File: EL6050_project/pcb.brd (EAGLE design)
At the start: 160 x 100 mm, 6 parts

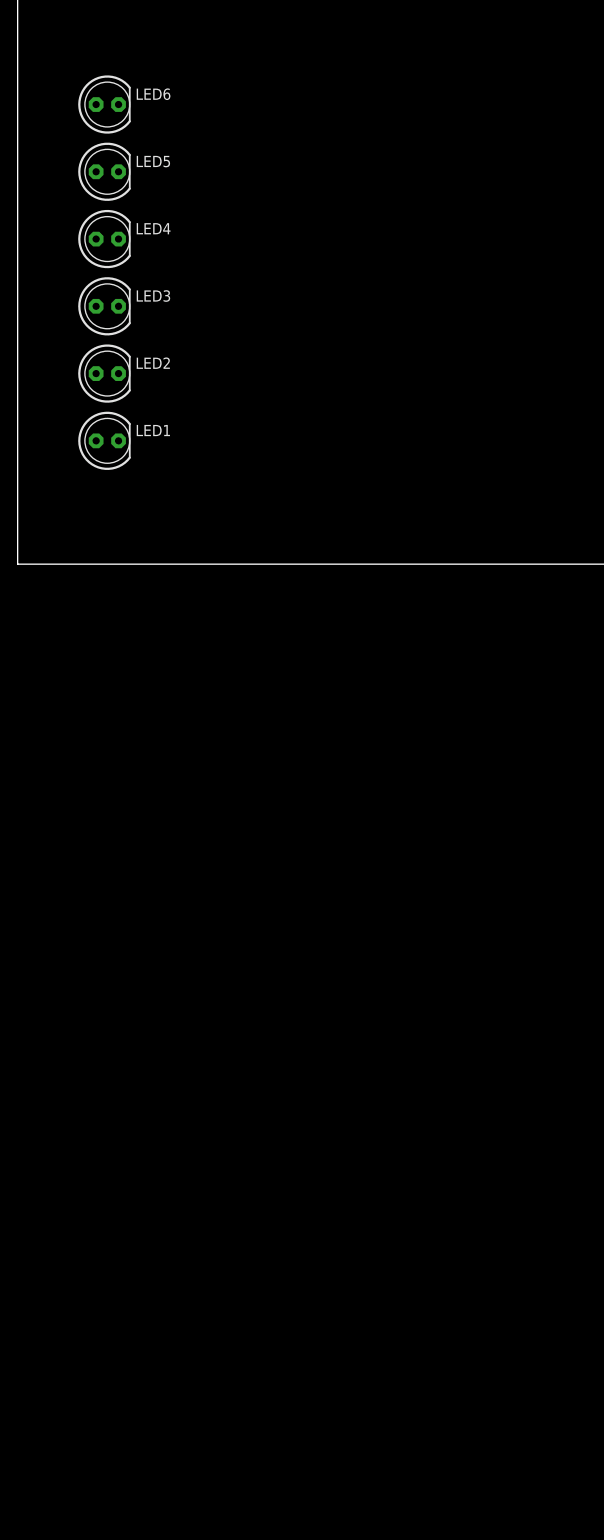
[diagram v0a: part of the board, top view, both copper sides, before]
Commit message: add lorawan module and arduino to schematic
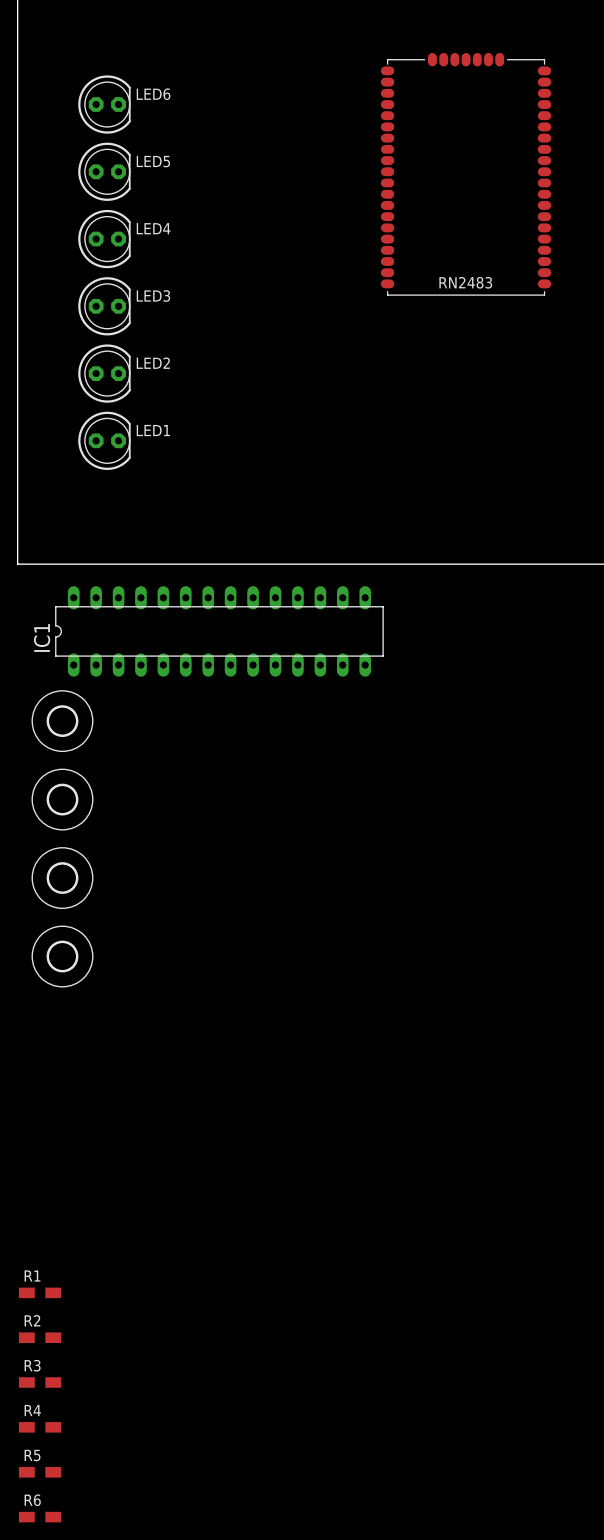
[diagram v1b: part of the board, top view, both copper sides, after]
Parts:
- added H1, H2, H3, H4: MOUNT-HOLE3.2, holes:3,2
- added IC1: MEGA8-P, atmel:DIL28-3
- added R1, R2, R3, R4, R5, R6: (no value), rcl:R1206W
- added U$1: MICROCHIP_RN2483, lora-lorawan-modules:MICROCHIP_RN2483
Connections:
- new net AVCC: IC1.20
- new net GND: IC1.22, IC1.8
- new net N$1: U$1.35
- new net N$10: U$1.39
- new net N$11: U$1.43
- new net N$12: U$1.45
- new net N$13: U$1.46
- new net N$14: U$1.10
- new net N$15: U$1.12, U$1.34
- new net N$16: U$1.32
- new net N$17: U$1.25
- new net N$18: U$1.3
- new net N$19: U$1.7
- new net N$2: U$1.36
- new net N$20: U$1.31
- new net N$21: U$1.1, U$1.11, U$1.20, U$1.21, U$1.22, U$1.24, U$1.26, U$1.27, U$1.28, U$1.33, U$1.41, U$1.47, U$1.8
- new net N$22: U$1.23
- new net N$23: U$1.2
- new net N$24: U$1.6
- new net N$25: U$1.30
- new net N$26: LED1.K
- new net N$27: LED2.K
- new net N$28: LED3.K
- new net N$29: LED4.K
- new net N$3: U$1.37
- new net N$30: LED5.K
- new net N$31: LED6.K
- new net N$32: LED1.A, R1.1
- new net N$33: LED2.A, R2.1
- new net N$34: LED3.A, R3.1
- new net N$35: LED4.A, R4.1
- new net N$36: LED5.A, R5.1
- new net N$37: LED6.A, R6.1
- new net N$38: IC1.23
- new net N$39: IC1.25
- new net N$4: U$1.38
- new net N$40: IC1.2
- new net N$41: IC1.4
- new net N$42: IC1.6
- new net N$43: IC1.12
- new net N$44: IC1.14
- new net N$45: IC1.17
- new net N$46: IC1.18
- new net N$47: IC1.27
- new net N$48: IC1.24
- new net N$49: IC1.26
- new net N$5: U$1.40
- new net N$50: IC1.28
- new net N$51: IC1.3
- new net N$52: IC1.5
- new net N$53: IC1.11
- new net N$54: IC1.13
- new net N$55: IC1.15
- new net N$56: IC1.16
- new net N$57: IC1.19
- new net N$6: U$1.44
- new net N$7: U$1.14
- new net N$8: U$1.13
- new net N$9: U$1.9
- new net VCC: IC1.7

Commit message: add and connect components
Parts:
- added C1, C2, C3, C4, C5, C6: (no value), rcl:C050-025X075
- added IC2: MEGA8-P, atmel:DIL28-3
- added Q1, Q2: (no value), crystal:HC18U-V
- added R10, R11, R7, R8: (no value), rcl:R1206W
- added R9: 10k, rcl:R1206W
- added SV1, SV2: (no value), con-lstb:MA03-1
- added X1: BU-SMA-V, con-coax:BU-SMA-V
- added X2: GMSTBA2, con-phoenix-762:GMSTBA2
- moved H1 150.3 mm to (146.1, 34.3)
- moved H2 150.3 mm to (146.1, 25.4)
- moved H3 150.3 mm to (146.1, 16.5)
- moved H4 150.3 mm to (146.1, 7.62)
- moved R4 131.8 mm to (26.7, 31.8)
- moved R5 131.8 mm to (26.7, 26.7)
- moved R1 131.8 mm to (26.7, 47.0)
- moved R2 131.8 mm to (26.7, 41.9)
- moved R3 131.8 mm to (26.7, 36.8)
- moved R6 131.8 mm to (26.7, 21.6)
- moved IC1 81.7 mm to (39.4, 72.4)
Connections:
- net AVCC renamed N$63
- new net 5V: C3.2, C6.2, IC1.7, IC2.7, R11.2, R8.2, SV1.1, SV2.1
- new net N$58: IC1.1, R8.1
- new net N$59: IC1.21
- new net N$60: C2.2, IC1.9, Q1.2, R7.2
- new net N$61: IC2.17
- new net N$62: IC1.22
- new net N$64: C1.2, IC1.10, Q1.1, R7.1
- new net N$65: IC2.18
- new net N$66: IC2.27
- new net N$67: IC2.24
- new net N$68: IC2.26
- new net N$69: IC2.28
- new net N$70: IC2.5
- new net N$71: IC2.11
- new net N$72: IC2.13
- new net N$73: IC2.15
- new net N$74: IC2.16
- new net N$75: IC2.19
- new net N$76: IC2.1, R11.1
- new net N$77: IC2.21
- new net N$78: C5.2, IC2.9, Q2.2, R10.2
- new net N$79: IC2.22
- new net N$80: IC2.20
- new net N$81: C4.2, IC2.10, Q2.1, R10.1
- new net RF_LRW: U$1.23, X1.1
- new net RX-LRW: IC1.2, IC2.2, U$1.6
- new net TX-LRW: IC1.3, IC2.3, U$1.7
- new net ULS1: SV1.3
- new net ULS2: SV2.3
- net GND: now also C1.1, C2.1, C3.1, C4.1, C5.1, C6.1, IC2.8, LED4.A, R1.2, R2.2, R3.2, R4.1, R4.2, R5.2, R6.2, SV1.2, SV2.2, U$1.1, U$1.11, U$1.20, U$1.21, U$1.22, U$1.24, U$1.26, U$1.27, U$1.28, U$1.33, U$1.41, U$1.47, U$1.8, X1.2, X1.3, X1.4, X1.5; no longer IC1.22
- net N$15: now also X2.1; no longer U$1.12, U$1.34
- net N$16: now also R9.2
- net N$19: now also X2.2; no longer U$1.7
- net N$21: now also IC2.23; no longer U$1.1, U$1.11, U$1.20, U$1.21, U$1.22, U$1.24, U$1.26, U$1.27, U$1.28, U$1.33, U$1.41, U$1.47, U$1.8
- net N$22: now also IC2.25; no longer U$1.23
- net N$24: now also IC2.4; no longer U$1.6
- net N$35: now also IC2.6; no longer LED4.A, R4.1
- net N$40: now also IC2.12; no longer IC1.2
- net N$51: now also IC2.14; no longer IC1.3
- net VCC: now also R9.1, U$1.12, U$1.34; no longer IC1.7

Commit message: all components added and board started
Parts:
- removed Q2: (no value), crystal:HC18U-V
- removed R10, R11: (no value), rcl:R1206W
- removed SV1, SV2: (no value), con-lstb:MA03-1
- removed U$1: MICROCHIP_RN2483, lora-lorawan-modules:MICROCHIP_RN2483
- removed X1: BU-SMA-V, con-coax:BU-SMA-V
- removed X2: GMSTBA2, con-phoenix-762:GMSTBA2
- added ANTENA: BU-SMA-V, con-coax:BU-SMA-V
- added C10: 100n, rcl:C050-024X044
- added C7: 100nF, rcl:C050-025X075
- added C8: 0.1u, rcl:C050-025X075
- added C9: 47u, rcl:E2,5-6E
- added D1: 1N4004, diode:DO41-10
- added FTDI: (no value), con-lstb:MA06-1
- added L1: 100mF, inductor-coilcraft2:MSS1260
- added LIDAR1, LIDAR2: (no value), sparkfun-connectors:JST-4-PTH
- added LRW-RN2903: MICROCHIP_RN2483, lora-lorawan-modules:MICROCHIP_RN2483
- added POWERSUPPLY: (no value), con-phoenix-500:MSTBV2
- C3, C4, C5, C6: value (none) -> 100nF
- IC1: value MEGA8-P -> ATMEGA2560-16AU; device atmel:DIL28-3 -> atmel-2005:TQFP100
- IC2: value MEGA8-P -> 7805T; device atmel:DIL28-3 -> linear:TO220H
- R7: value (none) -> 1M
- R8: value (none) -> 10k
- moved H2 148.6 mm to (5.08, 72.4)
- moved H1 144.0 mm to (5.08, 5.08)
- moved IC2 118.3 mm to (38.1, 64.8)
- moved C6 115.7 mm to (21.6, 44.5), turned to 180 degrees
- moved C5 108.5 mm to (44.5, 26.7), turned to 90 degrees
- moved C4 92.5 mm to (40.6, 26.7), turned to 90 degrees
- moved LED2 83.1 mm to (78.7, 68.6)
- moved H3 78.1 mm to (91.4, 72.4)
- moved R8 76.8 mm to (50.8, 50.8)
- moved LED4 75.1 mm to (81.3, 61.0)
- moved R4 73.9 mm to (91.4, 67.3)
- moved LED6 71.2 mm to (81.3, 49.5)
- moved R7 69.9 mm to (58.4, 38.1), turned to 270 degrees
- moved LED3 64.8 mm to (68.6, 57.1)
- moved R6 63.8 mm to (81.3, 54.6)
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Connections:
- removed net N$15: X2.1
- removed net N$16: R9.2, U$1.32
- removed net N$19: X2.2
- removed net N$24: IC2.4
- removed net N$26: LED1.K
- removed net N$27: LED2.K
- removed net N$28: LED3.K
- removed net N$29: LED4.K
- removed net N$30: LED5.K
- removed net N$31: LED6.K
- removed net N$35: IC2.6
- removed net N$40: IC2.12
- removed net N$43: IC1.12
- removed net N$51: IC2.14
- removed net N$58 (its old number): IC1.1, R8.1
- removed net N$61: IC2.17
- removed net N$65: IC2.18
- removed net N$66 (its old number): IC2.27
- removed net N$67: IC2.24
- removed net N$68: IC2.26
- removed net N$69 (its old number): IC2.28
- removed net N$70: IC2.5
- removed net N$71: IC2.11
- removed net N$72: IC2.13
- removed net N$73: IC2.15
- removed net N$74: IC2.16
- removed net N$75: IC2.19
- removed net N$76: IC2.1, R11.1
- removed net N$77: IC2.21
- removed net N$78: C5.2, IC2.9, Q2.2, R10.2
- removed net N$79: IC2.22
- removed net RF_LRW: U$1.23, X1.1
- removed net ULS1: SV1.3
- removed net ULS2: SV2.3
- removed net VCC: R9.1, U$1.12, U$1.34
- new net 3V3: FTDI.1, IC2.3, LRW-RN2903.12, LRW-RN2903.34, R9.1
- new net AVCC: C7.2, IC1.100, L1.1
- new net DST-CP: C8.1, FTDI.6
- new net L_DIST: IC1.40, LED6.K
- new net L_ON: IC1.42
- new net L_RED: IC1.41, LED2.K
- new net L_TRSA: IC1.39, LED3.K
- new net L_TRSB: IC1.38, LED4.K
- new net L_TRSC: IC1.37, LED5.K
- new net N$100: IC1.76
- new net N$101: IC1.78
- new net N$106: IC1.59
- new net N$107: IC1.57
- new net N$108: IC1.54
- new net N$109: IC1.53
- new net N$110: IC1.49
- new net N$111: IC1.47
- new net N$113: IC1.43
- new net N$114: IC1.8
- new net N$118: IC1.91
- new net N$119: IC1.93
- new net N$120: IC1.95
- new net N$121: IC1.97
- new net N$122: IC1.29
- new net N$123: IC1.70
- new net N$124: IC1.51
- new net N$125: IC1.55
- new net N$126: IC1.50
- new net N$127: IC1.48
- new net N$129: IC1.44
- new net N$130: IC1.9
- new net N$131: IC1.7
- new net N$134: IC1.90
- new net N$135: IC1.92
- new net N$136: IC1.94
- new net N$137: IC1.96
- new net N$138: IC1.1
- new net N$140: IC1.52
- new net N$41: C1.2, IC1.34, Q1.1, R7.1
- new net N$42: C2.2, IC1.33, Q1.2, R7.2
- new net N$46: IC1.36
- new net N$47: IC1.82
- new net N$48: IC1.84
- new net N$49: IC1.86
- new net N$50: IC1.88
- new net N$52: IC1.79
- new net N$62: IC1.73
- new net N$63: IC1.75
- new net N$84: IC1.60
- new net N$85: IC1.58
- new net N$86: IC1.56
- new net N$87: IC1.85
- new net N$88: IC1.87
- new net N$89: IC1.89
- new net N$90: IC1.69
- new net N$91: IC1.67
- new net N$92: IC1.65
- new net N$98: IC1.72
- new net N$99: IC1.74
- new net PWRIN: D1.A, POWERSUPPLY.1
- new net RF-LRW: ANTENA.1, LRW-RN2903.23
- new net RST-LRW: LRW-RN2903.32, R9.2
- new net RX-CP: FTDI.5, IC1.64
- new net RX-LID1: IC1.46, LIDAR1.2
- new net RX-LID2: IC1.13, LIDAR2.2
- new net TX-CP: FTDI.4, IC1.63
- new net TX-LID1: IC1.45, LIDAR1.1
- new net TX-LID2: IC1.12, LIDAR2.1
- net 5V: now also C10.1, C4.2, C5.2, C9.+, D1.C, FTDI.3, IC1.10, IC1.31, IC1.61, IC1.80, IC2.1, L1.2, LED1.K, LIDAR1.3, LIDAR2.3, R8.1; no longer C6.2, IC1.7, IC2.7, R11.2, R8.2, SV1.1, SV2.1
- net GND: now also ANTENA.2, ANTENA.3, ANTENA.4, ANTENA.5, C10.2, C6.2, C7.1, C9.-, FTDI.2, IC1.11, IC1.32, IC1.62, IC1.81, IC1.99, IC2.2, LIDAR1.4, LIDAR2.4, LRW-RN2903.1, LRW-RN2903.11, LRW-RN2903.20, LRW-RN2903.21, LRW-RN2903.22, LRW-RN2903.24, LRW-RN2903.26, LRW-RN2903.27, LRW-RN2903.28, LRW-RN2903.33, LRW-RN2903.41, LRW-RN2903.47, LRW-RN2903.8, POWERSUPPLY.2; no longer C6.1, IC1.8, IC2.8, SV1.2, SV2.2, U$1.1, U$1.11, U$1.20, U$1.21, U$1.22, U$1.24, U$1.26, U$1.27, U$1.28, U$1.33, U$1.41, U$1.47, U$1.8, X1.2, X1.3, X1.4, X1.5
- net N$1: now also LRW-RN2903.35; no longer U$1.35
- net N$10: now also LRW-RN2903.39; no longer U$1.39
- net N$11: now also LRW-RN2903.43; no longer U$1.43
- net N$12: now also LRW-RN2903.45; no longer U$1.45
- net N$13: now also LRW-RN2903.46; no longer U$1.46
- net N$14: now also LRW-RN2903.10; no longer U$1.10
- net N$17: now also LRW-RN2903.25; no longer U$1.25
- net N$18: now also LRW-RN2903.3; no longer U$1.3
- net N$2: now also LRW-RN2903.36; no longer U$1.36
- net N$20: now also LRW-RN2903.31; no longer U$1.31
- net N$21: now also C8.2, IC1.30, R8.2; no longer IC2.23
- net N$22: now also C6.1, IC1.98; no longer IC2.25
- net N$23: now also LRW-RN2903.2; no longer U$1.2
- net N$25: now also LRW-RN2903.30; no longer U$1.30
- net N$3: now also LRW-RN2903.37; no longer U$1.37
- net N$4: now also LRW-RN2903.38; no longer U$1.38
- net N$5: now also LRW-RN2903.40; no longer U$1.40
- net N$53: now also IC1.68; no longer IC1.11
- net N$54: now also IC1.66; no longer IC1.13
- net N$6: now also LRW-RN2903.44; no longer U$1.44
- net N$60: now also IC1.71; no longer C2.2, IC1.9, Q1.2, R7.2
- net N$64: now also IC1.77; no longer C1.2, IC1.10, Q1.1, R7.1
- net N$7: now also LRW-RN2903.14; no longer U$1.14
- net N$8: now also LRW-RN2903.13; no longer U$1.13
- net N$80: now also IC1.35; no longer IC2.20
- net N$81: now also IC1.83; no longer C4.2, IC2.10, Q2.1, R10.1
- net N$9: now also LRW-RN2903.9; no longer U$1.9
- net RX-LRW: now also IC1.3, LRW-RN2903.7; no longer IC1.2, IC2.2, U$1.6
- net TX-LRW: now also IC1.2, LRW-RN2903.6; no longer IC1.3, IC2.3, U$1.7
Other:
- board size 160 x 100 mm -> 96.5 x 78.4 mm

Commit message: end board and update schematic
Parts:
- removed LED1, LED2, LED3, LED4, LED5, LED6: (no value), adafruit:LED5MM
- removed POWERSUPPLY: (no value), con-phoenix-500:MSTBV2
- added C11, C12: 10u, rcl:E2,5-6E
- added D2, D3, D4, D5, D6, D7, D8, D9: 1N4004, diode:DO41-10
- added IC3: 7805T, linear:TO220H
- added J1: DCJ0202, con-jack:DCJ0202
- added L_5V, L_DIST, L_RED, L_TRSA, L_TRSB, L_TRSC: (no value), adafruit:LED5MM
- added R10, R11: 10k, rcl:R1206W
- added TRSA, TRSB, TRSC: (no value), sparkfun-connectors:JST-4-PTH
- added U1: LM358, sparkfun-amplifiers:DIP08
- C1, C2: value (none) -> 22p
- C10: value 100n -> 47u; device rcl:C050-024X044 -> rcl:E2,5-6E
- C3, C4, C5, C6, C7: value 100nF -> 100n
- C8: value 0.1u -> 100n
- L1: value 100mF -> 10u
- Q1: value (none) -> 16MHz
- R1, R2, R3, R4, R5, R6: value (none) -> 100
- moved R2 62.9 mm to (48.6, 18.4)
- moved R4 52.4 mm to (72.7, 18.4)
- moved R6 44.0 mm to (56.2, 18.4)
- moved R3 44.0 mm to (65.1, 18.4)
- moved D1 39.7 mm to (28.3, 17.1), turned to 0 degrees
- moved IC2 35.7 mm to (9.21, 43.8)
- moved R5 35.6 mm to (80.3, 18.4)
- moved C9 32.0 mm to (14.3, 23.5), turned to 270 degrees
- moved C10 31.3 mm to (4.13, 23.5), turned to 270 degrees
- moved LRW-RN2903 30.4 mm to (18.1, 42.5)
- moved R9 28.1 mm to (14.3, 60.3)
- moved FTDI 21.2 mm to (74.0, 69.5)
- moved LIDAR1 19.7 mm to (87.9, 24.8)
- moved C6 19.6 mm to (41.0, 41.3), turned to 270 degrees
- moved C7 19.6 mm to (44.8, 41.3)
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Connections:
- net N$21 renamed RESET
- net N$41 renamed XTAL1
- net N$42 renamed XTAL2
- removed net N$108: IC1.54
- removed net N$109: IC1.53
- removed net N$125: IC1.55
- new net -15V: R11.2, TRSA.3, TRSB.3, TRSC.3, U1.1
- new net 15V: C10.+, D2.C, D3.C, IC2.1, R10.1, TRSA.4, TRSB.4, TRSC.4, U1.8
- new net N$15: R10.2, R11.1, U1.2
- new net N$16: L_TRSB.A, R4.1
- new net VO_A: D4.C, D5.A, IC1.55, TRSA.2
- new net VO_B: D6.C, D7.A, IC1.54, TRSB.2
- new net VO_C: D8.C, D9.A, IC1.53, TRSC.2
- net 3V3: now also C11.+, D1.A, IC3.3; no longer IC2.3
- net 5V: now also C12.+, D2.A, D5.C, D7.C, D9.C, IC2.3, IC3.1, L_5V.K; no longer C10.1, IC2.1, LED1.K
- net GND: now also C10.-, C11.-, C12.-, D4.A, D6.A, D8.A, IC3.2, J1.2, J1.3, TRSA.1, TRSB.1, TRSC.1, U1.3, U1.4; no longer C10.2, LED4.A, POWERSUPPLY.2, R4.1
- net L_DIST: now also L_DIST.K; no longer LED6.K
- net L_RED: now also L_RED.K; no longer LED2.K
- net L_TRSA: now also L_TRSA.K; no longer LED3.K
- net L_TRSB: now also L_TRSB.K; no longer LED4.K
- net L_TRSC: now also L_TRSC.K; no longer LED5.K
- net N$32: now also L_5V.A; no longer LED1.A
- net N$33: now also L_RED.A; no longer LED2.A
- net N$34: now also L_TRSA.A; no longer LED3.A
- net N$36: now also L_TRSC.A; no longer LED5.A
- net N$37: now also L_DIST.A; no longer LED6.A
- net PWRIN: now also D3.A, J1.1; no longer D1.A, POWERSUPPLY.1
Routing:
- net GND: track 0.00 -> 465.3 mm, vias 0 -> 1
- net 5V: track 0.00 -> 309.9 mm, vias 0 -> 1
- net 15V: track 0.00 -> 146.5 mm, vias 0 -> 1
- net 3V3: track 0.00 -> 122.8 mm, vias 0 -> 1
- net VO_C: track 0.00 -> 71.4 mm
- net L_TRSA: track 0.00 -> 71.0 mm, vias 0 -> 1
- net L_TRSC: track 0.00 -> 70.8 mm, vias 0 -> 1
- net L_TRSB: track 0.00 -> 65.8 mm, vias 0 -> 1
- net RX-LID1: track 0.00 -> 63.7 mm, vias 0 -> 1
- net TX-LID2: track 0.00 -> 60.5 mm
- net TX-LID1: track 0.00 -> 60.4 mm, vias 0 -> 1
- net -15V: track 0.00 -> 60.0 mm, vias 0 -> 1
- net RX-LID2: track 0.00 -> 59.6 mm
- net VO_B: track 0.00 -> 56.1 mm, vias 0 -> 1
- net L_RED: track 0.00 -> 54.6 mm, vias 0 -> 1
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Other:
- board size 96.5 x 78.4 mm -> 91.7 x 73.3 mm
